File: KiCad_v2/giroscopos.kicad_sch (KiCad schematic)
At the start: 15 parts, among them U4 MPU-6050, U5 BNO085

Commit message: feat: agrego 3d de ESP32 Y CM4
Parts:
- U5: footprint Footprint KiCad:IC_BNO085 -> Custom_Footprints:IC_BNO085
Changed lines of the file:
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@@
 			)
 		)
-		(property "Footprint" "Footprint KiCad:IC_BNO085"
+		(property "Footprint" "Custom_Footprints:IC_BNO085"
 			(at 88.9 104.14 0)
 			(effects

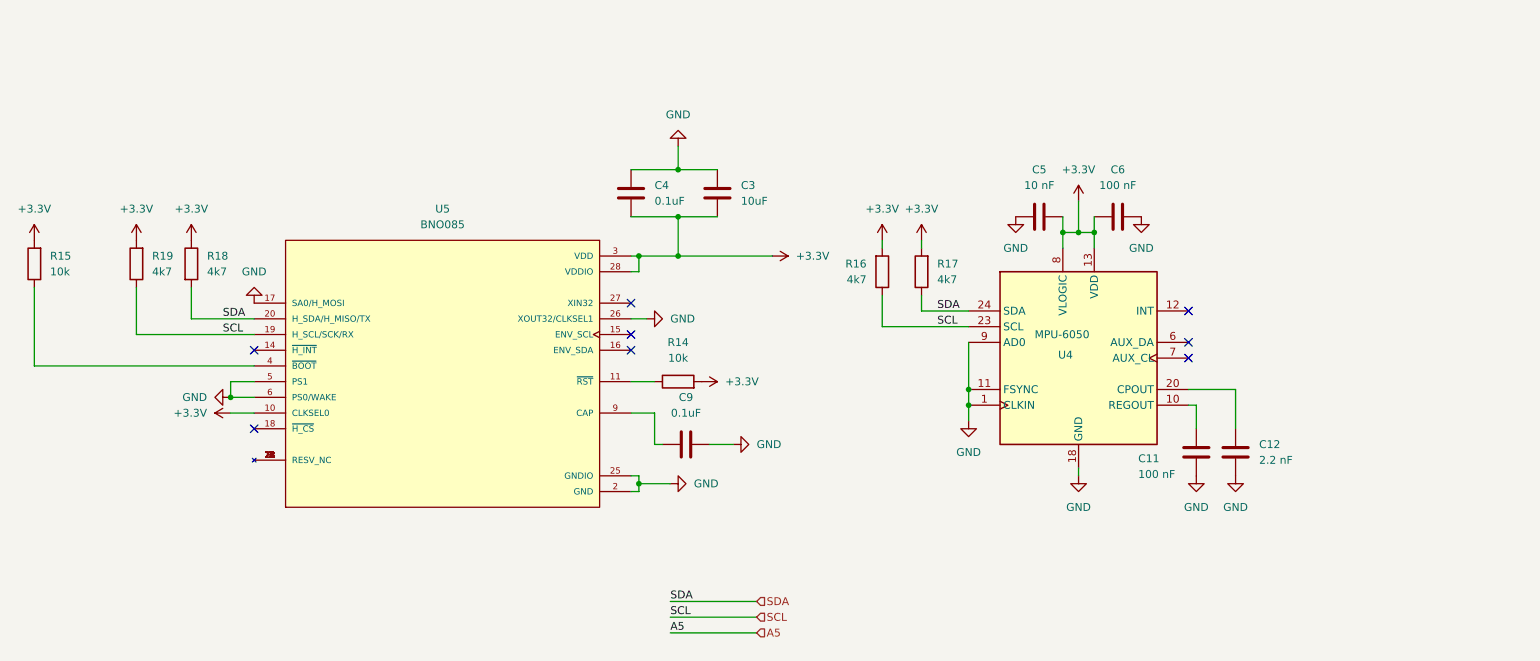
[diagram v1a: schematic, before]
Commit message: agrego step up para 3A con su debido esquematico
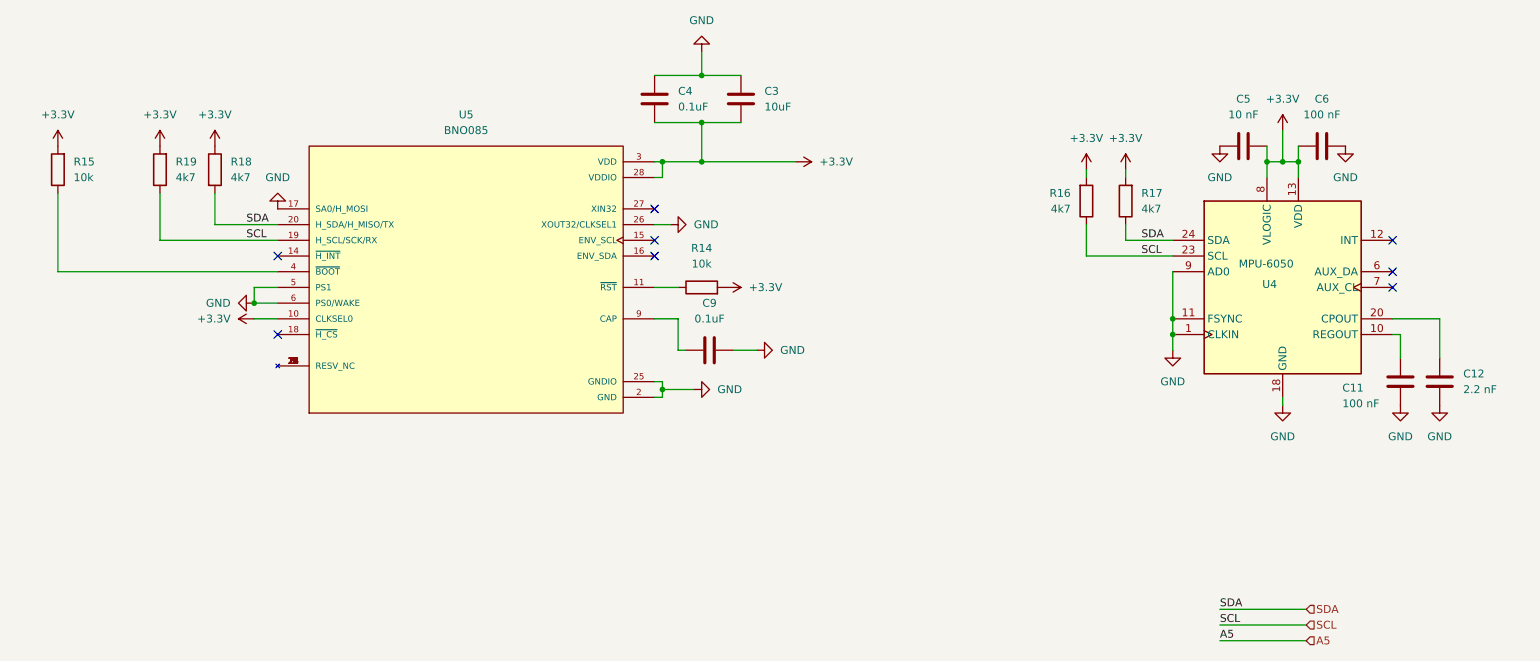
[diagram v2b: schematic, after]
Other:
- moved on the sheet: C11, C12, C3, C4, C5, C6, C9, R14, R15, R16, R17, R18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

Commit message: agrego boton de wake
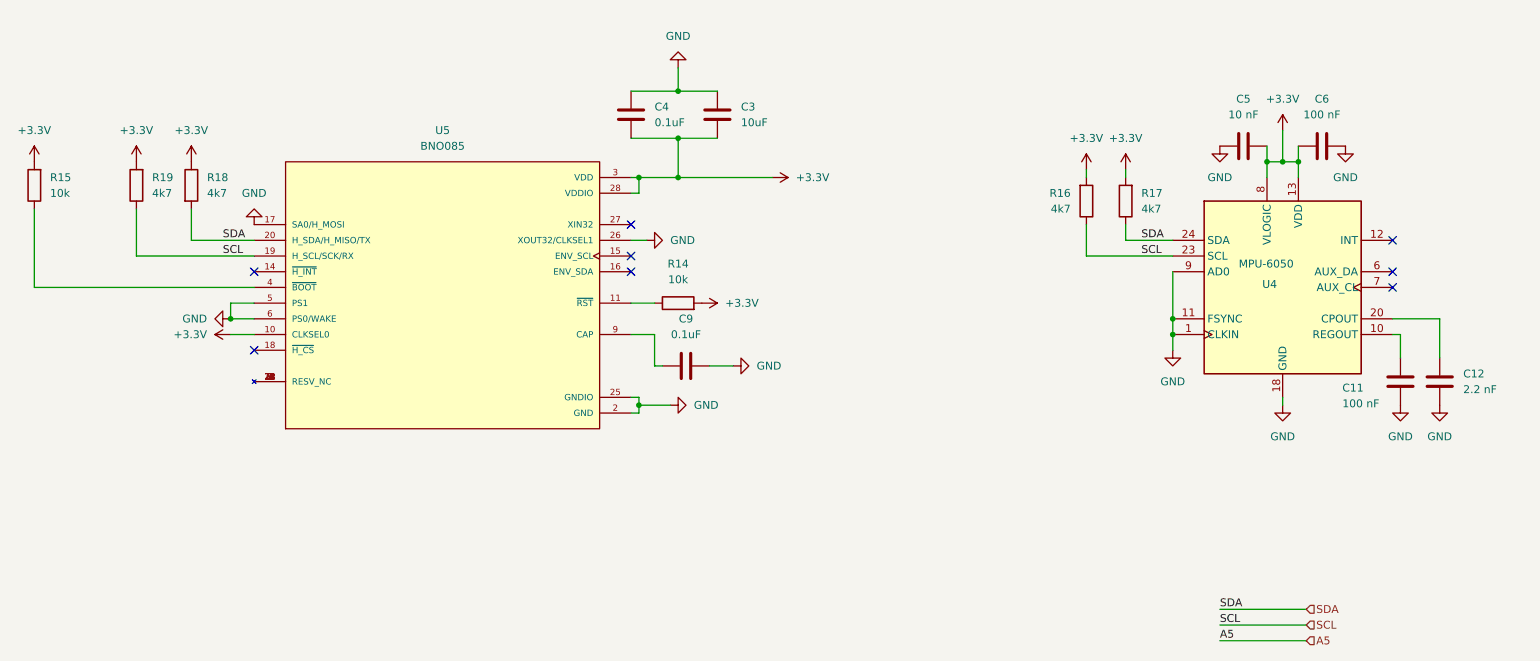
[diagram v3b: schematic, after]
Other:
- moved on the sheet: C3, C4, C9, R14, R15, R18, R19, U5

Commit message: Resistencias calculadas, esquematico terminado
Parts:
- C11, C12, C3, C4, C5, C6, C9: footprint Capacitor_SMD:C_0805_2012Metric -> Capacitor_SMD:C_0603_1608Metric
- R14, R15, R16, R17, R18, R19: footprint Resistor_SMD:R_0805_2012Metric -> Resistor_SMD:R_0603_1608Metric
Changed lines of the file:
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@@
 			)
 		)
-		(property "Footprint" "Capacitor_SMD:C_0805_2012Metric"
+		(property "Footprint" "Capacitor_SMD:C_0603_1608Metric"
 			(at 251.1552 110.49 0)
 			(effects
@@
 			)
 		)
-		(property "Footprint" "Capacitor_SMD:C_0805_2012Metric"
+		(property "Footprint" "Capacitor_SMD:C_0603_1608Metric"
 			(at 120.3452 67.31 0)
 			(effects
@@
 			)
 		)
-		(property "Footprint" "Resistor_SMD:R_0805_2012Metric"
+		(property "Footprint" "Resistor_SMD:R_0603_1608Metric"
 			(at 201.168 77.47 90)
 			(effects
@@
 			)
 		)
-		(property "Footprint" "Capacitor_SMD:C_0805_2012Metric"
+		(property "Footprint" "Capacitor_SMD:C_0603_1608Metric"
 			(at 234.95 67.6148 0)
 			(effects
@@
 			)
 		)
-		(property "Footprint" "Capacitor_SMD:C_0805_2012Metric"
+		(property "Footprint" "Capacitor_SMD:C_0603_1608Metric"
 			(at 134.3152 67.31 0)
 			(effects
@@
 			)
 		)
-		(property "Footprint" "Capacitor_SMD:C_0805_2012Metric"
+		(property "Footprint" "Capacitor_SMD:C_0603_1608Metric"
 			(at 132.08 103.1748 0)
 			(effects
@@
 			)
 		)
-		(property "Footprint" "Resistor_SMD:R_0805_2012Metric"
+		(property "Footprint" "Resistor_SMD:R_0603_1608Metric"
 			(at 191.262 77.47 90)
 			(effects
@@
 			)
 		)
-		(property "Footprint" "Resistor_SMD:R_0805_2012Metric"
+		(property "Footprint" "Resistor_SMD:R_0603_1608Metric"
 			(at 41.148 74.93 90)
 			(effects
@@
 			)
 		)
-		(property "Footprint" "Resistor_SMD:R_0805_2012Metric"
+		(property "Footprint" "Resistor_SMD:R_0603_1608Metric"
 			(at 24.638 74.93 90)
 			(effects
@@
 			)
 		)
-		(property "Footprint" "Capacitor_SMD:C_0805_2012Metric"
+		(property "Footprint" "Capacitor_SMD:C_0603_1608Metric"
 			(at 244.8052 110.49 0)
 			(effects
@@
 			)
 		)
-		(property "Footprint" "Resistor_SMD:R_0805_2012Metric"
+		(property "Footprint" "Resistor_SMD:R_0603_1608Metric"
 			(at 46.482 74.93 90)
 			(effects
@@
 			)
 		)
-		(property "Footprint" "Capacitor_SMD:C_0805_2012Metric"
+		(property "Footprint" "Capacitor_SMD:C_0603_1608Metric"
 			(at 222.25 67.6148 0)
 			(effects
@@
 			)
 		)
-		(property "Footprint" "Resistor_SMD:R_0805_2012Metric"
+		(property "Footprint" "Resistor_SMD:R_0603_1608Metric"
 			(at 127 95.758 90)
 			(effects

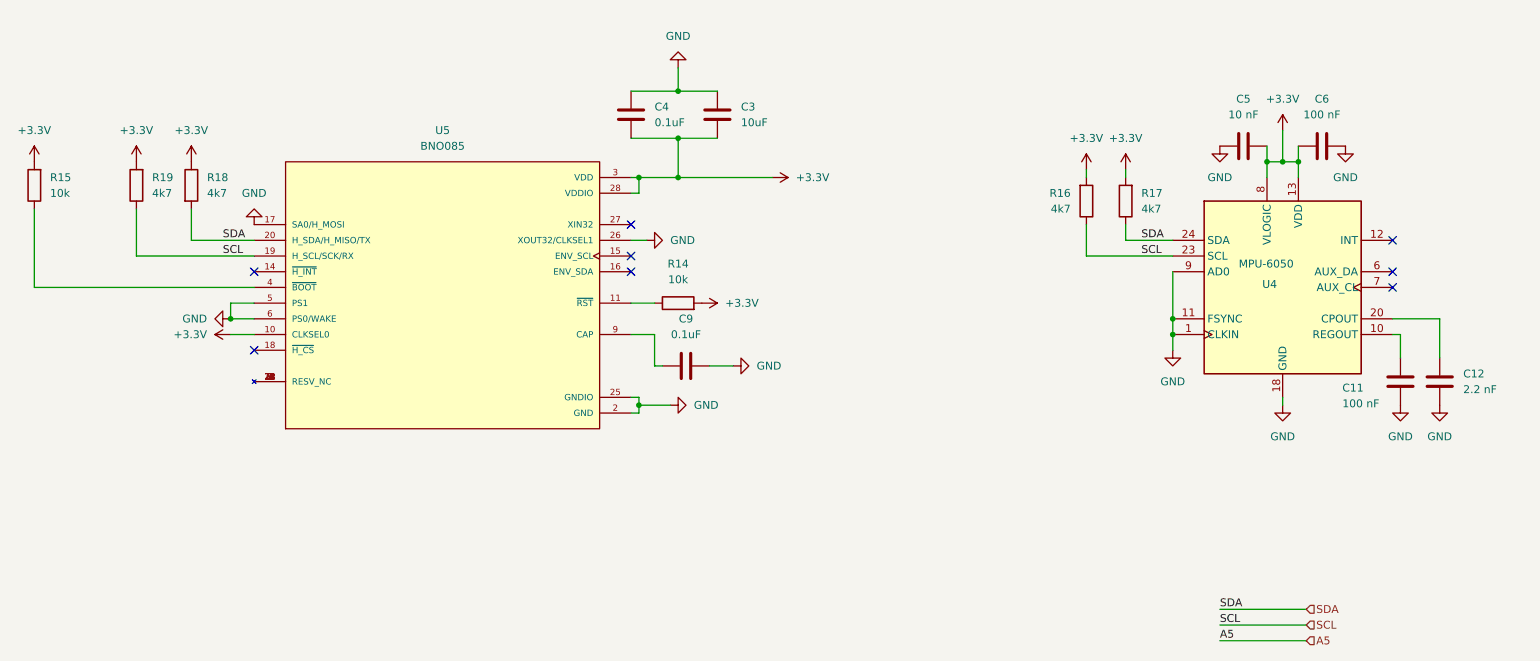
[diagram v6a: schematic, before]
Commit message: feat: comienzo rooteo y perfeccionar esquematico
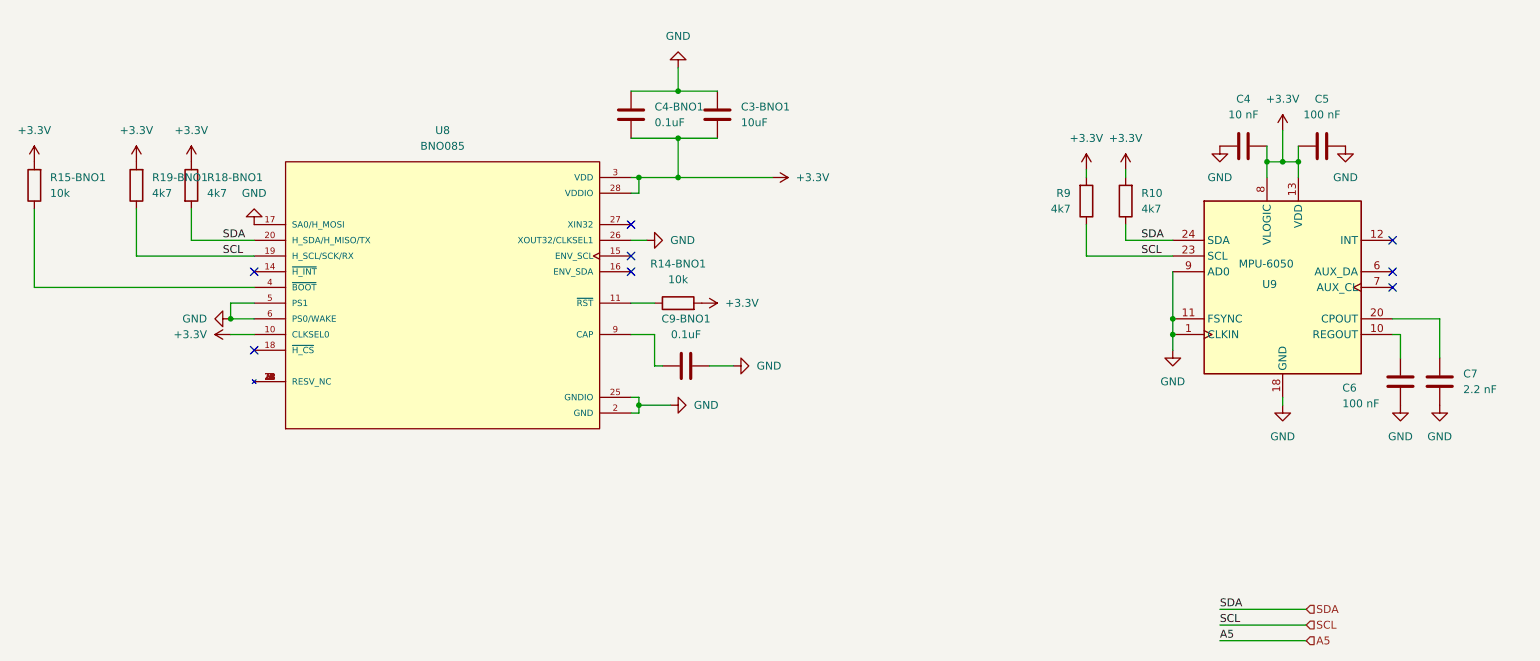
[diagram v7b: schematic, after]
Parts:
- renumbered C3 to C3-BNO1, C5 to C4, C4 to C4-BNO1, C6 to C5, C11 to C6, C12 to C7, C9 to C9-BNO1, R17 to R10, R14 to R14-BNO1, R15 to R15-BNO1, R18 to R18-BNO1, R19 to R19-BNO1, R16 to R9, U5 to U8, U4 to U9
